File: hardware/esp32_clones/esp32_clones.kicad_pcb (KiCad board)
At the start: 2 copper layers, 110 x 60 mm, 27 parts, among them J2 USB_A, J3 USB_A, J4 USB_A, J5 Micro_SD_Card, J6 Barrel_Jack, J7 DA15_Pins, J9 AudioJack2_Ground

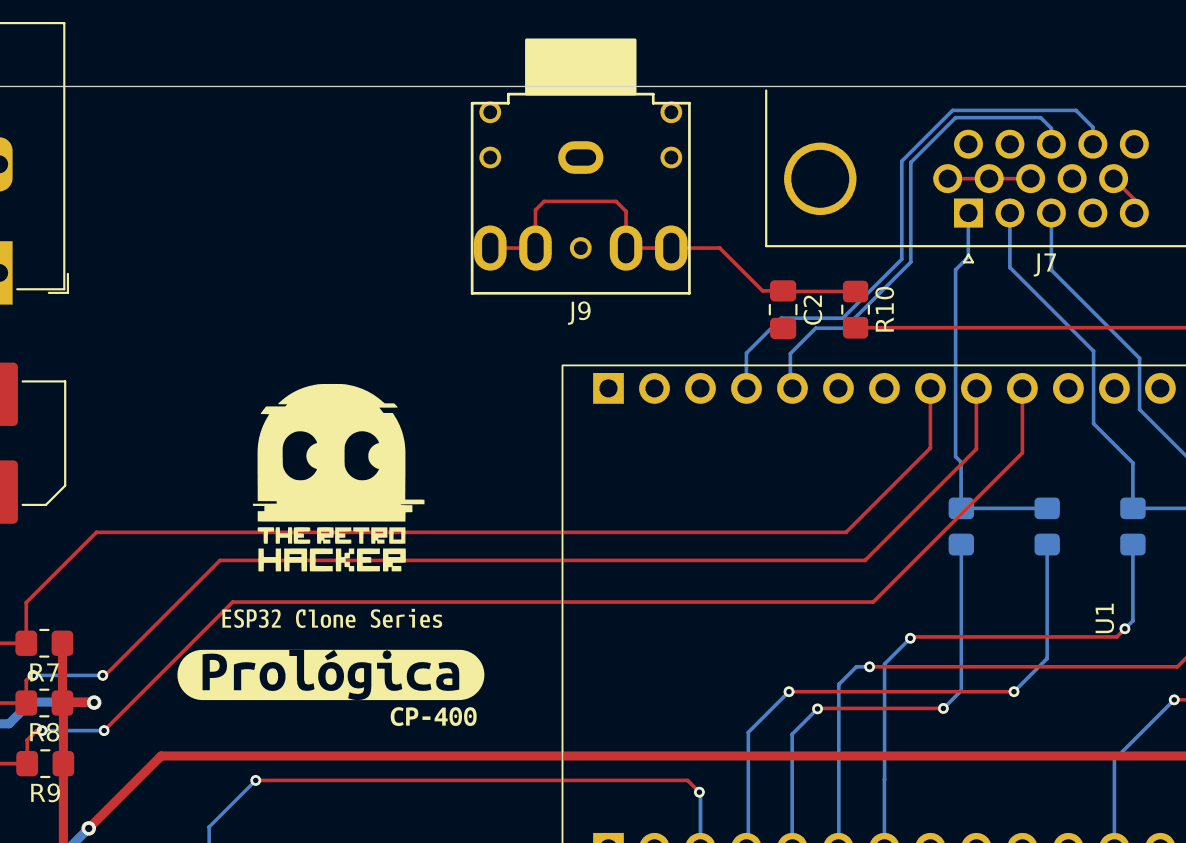
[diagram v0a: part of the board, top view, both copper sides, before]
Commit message: ## 1.11 - 2026-08-19
### Added

- Added a progress gauge that runs while a firmware update is validated and copied.

### Changed

- Moved the USB keyboard port to GPIO11 and GPIO12, joystick 1 to GPIO15 and GPIO16, and joystick 2 to GPIO17 and GPIO18, to simplify cable routing on the board.
- Gave every F12 screen the same layout, with the product name and screen title in the header, matching separator lines, and key hints in the footer. The disk image picker, firmware update screens, and error messages previously used their own styles.
- Renamed the "Joystick calibration" menu entry to "Joystick setup".
- Turned the joystick Serial debug output off by default.
- Listed only files with a matching extension when choosing a firmware or disk image, hiding folders such as System Volume Information that could not be opened anyway.
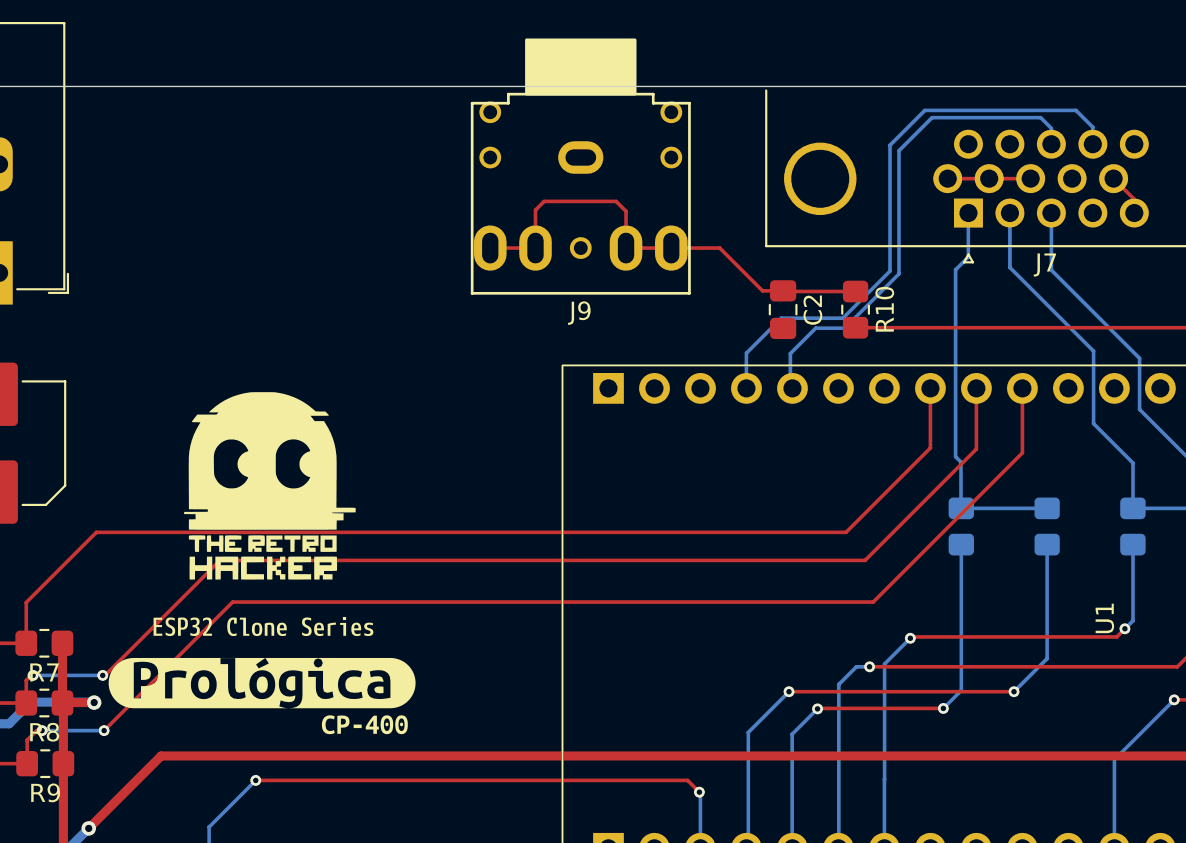
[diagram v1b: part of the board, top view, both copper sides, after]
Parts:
- moved G*** 3.83 mm to (124.6, 82.4)
- moved kibuzzard-6A32A22E 3.83 mm to (124.5, 93.0)
- moved kibuzzard-6A32A25A 3.83 mm to (124.5, 89.8)
- moved kibuzzard-6A32A222 3.83 mm to (130.2, 95.2)
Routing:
- net Net-(J7-P14): track 31.1 -> 32.0 mm
- net Net-(J7-P13): track 26.1 -> 26.9 mm
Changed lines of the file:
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@@
 	(footprint "kibuzzard-6A32A25A"
 		(layer "F.Cu")
-		(at 128.35 89.375)
+		(at 124.55 89.825)
 		(descr "Generated with KiBuzzard")
 		(tags "kb_params=eyJBbGlnbm1lbnRDaG9pY2UiOiAiQ2VudGVyIiwgIkNhcExlZnRDaG9pY2UiOiAiKCIsICJDYXBSaWdodENob2ljZSI6ICIpIiwgIkZvbnRDb21ib0JveCI6ICJtcGx1cy0xbW4tbWVkaXVtIiwgIkhlaWdodEN0cmwiOiAxLjAsICJMYXllckNvbWJvQm94IjogIkYuU2lsa1MiLCAiTGluZVNwYWNpbmdDdHJsIjogMTUuMCwgIk11bHRpTGluZVRleHQiOiAiRVNQMzIgQ2xvbmUgU2VyaWVzIiwgIlBhZGRpbmdCb3R0b21DdHJsIjogMC4wLCAiUGFkZGluZ0xlZnRDdHJsIjogMC4wLCAiUGFkZGluZ1JpZ2h0Q3RybCI6IDAuMCwgIlBhZGRpbmdUb3BDdHJsIjogMC4wLCAiV2lkdGhDdHJsIjogMC4wLCAiYWR2YW5jZWRDaGVja2JveCI6IHRydWUsICJpbmxpbmVGb3JtYXRUZXh0Ym94IjogdHJ1ZSwgImxpbmVvdmVyU3R5bGVDaG9pY2UiOiAiU3F1YXJlIiwgImxpbmVvdmVyVGhpY2tuZXNzQ3RybCI6IDV9")
@@
 	(footprint "TRH:TRH_NEW"
 		(layer "F.Cu")
-		(at 128.425 81.95)
+		(at 124.625 82.4)
 		(property "Reference" "G***"
 			(at 0 0 0)
@@
 	(footprint "kibuzzard-6A32A222"
 		(layer "F.Cu")
-		(at 133.95 94.8)
+		(at 130.15 95.25)
 		(descr "Generated with KiBuzzard")
 		(tags "kb_params=eyJBbGlnbm1lbnRDaG9pY2UiOiAiQ2VudGVyIiwgIkNhcExlZnRDaG9pY2UiOiAiKCIsICJDYXBSaWdodENob2ljZSI6ICIpIiwgIkZvbnRDb21ib0JveCI6ICJVYnVudHVNb25vLUIiLCAiSGVpZ2h0Q3RybCI6IDEuMCwgIkxheWVyQ29tYm9Cb3giOiAiRi5TaWxrUyIsICJMaW5lU3BhY2luZ0N0cmwiOiAxNS4wLCAiTXVsdGlMaW5lVGV4dCI6ICJDUC00MDAiLCAiUGFkZGluZ0JvdHRvbUN0cmwiOiAwLjAsICJQYWRkaW5nTGVmdEN0cmwiOiAwLjAsICJQYWRkaW5nUmlnaHRDdHJsIjogMC4wLCAiUGFkZGluZ1RvcEN0cmwiOiAwLjAsICJXaWR0aEN0cmwiOiAwLjAsICJhZHZhbmNlZENoZWNrYm94IjogdHJ1ZSwgImlubGluZUZvcm1hdFRleHRib3giOiB0cnVlLCAibGluZW92ZXJTdHlsZUNob2ljZSI6ICJTcXVhcmUiLCAibGluZW92ZXJUaGlja25lc3NDdHJsIjogNX0=")
@@
 	(footprint "kibuzzard-6A32A22E"
 		(layer "F.Cu")
-		(at 128.275 92.5)
+		(at 124.475 92.95)
 		(descr "Generated with KiBuzzard")
 		(tags "kb_params=eyJBbGlnbm1lbnRDaG9pY2UiOiAiQ2VudGVyIiwgIkNhcExlZnRDaG9pY2UiOiAiKCIsICJDYXBSaWdodENob2ljZSI6ICIpIiwgIkZvbnRDb21ib0JveCI6ICJVYnVudHVNb25vLUIiLCAiSGVpZ2h0Q3RybCI6IDIuMCwgIkxheWVyQ29tYm9Cb3giOiAiRi5TaWxrUyIsICJMaW5lU3BhY2luZ0N0cmwiOiAxNS4wLCAiTXVsdGlMaW5lVGV4dCI6ICJQcm9sXHUwMGYzZ2ljYSIsICJQYWRkaW5nQm90dG9tQ3RybCI6IDAuMCwgIlBhZGRpbmdMZWZ0Q3RybCI6IDAuMCwgIlBhZGRpbmdSaWdodEN0cmwiOiAwLjAsICJQYWRkaW5nVG9wQ3RybCI6IDAuMCwgIldpZHRoQ3RybCI6IDAuMCwgImFkdmFuY2VkQ2hlY2tib3giOiB0cnVlLCAiaW5saW5lRm9ybWF0VGV4dGJveCI6IGZhbHNlLCAibGluZW92ZXJTdHlsZUNob2ljZSI6ICJTcXVhcmUiLCAibGluZW92ZXJUaGlja25lc3NDdHJsIjogNX0=")
@@
 	)
 	(segment
-		(start 169.425 61.325)
-		(end 170.355 62.255)
+		(start 161.475 61.725)
+		(end 159.65 63.55)
 		(width 0.2)
 		(layer "B.Cu")
-		(net "Net-(J7-P14)")
+		(net "Net-(J7-P13)")
 	)
 	(segment
-		(start 151.225 76.675)
-		(end 151.225 74.725)
+		(start 153.65 74.75)
+		(end 153.65 76.56)
 		(width 0.2)
 		(layer "B.Cu")
-		(net "Net-(J7-P14)")
+		(net "Net-(J7-P13)")
 	)
 	(segment
-		(start 151.225 74.725)
-		(end 153.15 72.8)
+		(start 153.65 76.56)
+		(end 153.765 76.675)
 		(width 0.2)
 		(layer "B.Cu")
-		(net "Net-(J7-P14)")
+		(net "Net-(J7-P13)")
 	)
 	(segment
-		(start 162.609315 61.325)
-		(end 169.425 61.325)
+		(start 159.65 70.35)
+		(end 156.65 73.35)
 		(width 0.2)
 		(layer "B.Cu")
-		(net "Net-(J7-P14)")
+		(net "Net-(J7-P13)")
 	)
 	(segment
-		(start 153.15 72.8)
-		(end 156.55 72.8)
+		(start 159.65 63.55)
+		(end 159.65 70.35)
 		(width 0.2)
 		(layer "B.Cu")
-		(net "Net-(J7-P14)")
+		(net "Net-(J7-P13)")
 	)
 	(segment
-		(start 156.55 72.8)
-		(end 159.8 69.55)
+		(start 168.065 63.19)
+		(end 168.065 62.315)
 		(width 0.2)
 		(layer "B.Cu")
-		(net "Net-(J7-P14)")
+		(net "Net-(J7-P13)")
 	)
 	(segment
-		(start 170.355 62.255)
-		(end 170.355 63.19)
+		(start 156.65 73.35)
+		(end 155.05 73.35)
 		(width 0.2)
 		(layer "B.Cu")
-		(net "Net-(J7-P14)")
+		(net "Net-(J7-P13)")
 	)
 	(segment
-		(start 159.8 69.55)
-		(end 159.8 64.134315)
+		(start 155.05 73.35)
+		(end 153.65 74.75)
 		(width 0.2)
 		(layer "B.Cu")
-		(net "Net-(J7-P14)")
+		(net "Net-(J7-P13)")
 	)
 	(segment
-		(start 159.8 64.134315)
-		(end 162.609315 61.325)
+		(start 167.475 61.725)
+		(end 161.475 61.725)
 		(width 0.2)
 		(layer "B.Cu")
-		(net "Net-(J7-P14)")
+		(net "Net-(J7-P13)")
 	)
 	(segment
-		(start 153.65 74.75)
-		(end 153.65 76.56)
+		(start 168.065 62.315)
+		(end 167.475 61.725)
 		(width 0.2)
 		(layer "B.Cu")
@@
 	)
 	(segment
-		(start 162.775 61.725)
-		(end 160.3 64.2)
+		(start 153.15 72.8)
+		(end 156.55 72.8)
 		(width 0.2)
 		(layer "B.Cu")
-		(net "Net-(J7-P13)")
+		(net "Net-(J7-P14)")
 	)
 	(segment
-		(start 153.65 76.56)
-		(end 153.765 76.675)
+		(start 161.075 61.325)
+		(end 169.425 61.325)
 		(width 0.2)
 		(layer "B.Cu")
-		(net "Net-(J7-P13)")
+		(net "Net-(J7-P14)")
 	)
 	(segment
-		(start 155.05 73.35)
-		(end 153.65 74.75)
+		(start 169.425 61.325)
+		(end 170.355 62.255)
 		(width 0.2)
 		(layer "B.Cu")
-		(net "Net-(J7-P13)")
+		(net "Net-(J7-P14)")
 	)
 	(segment
-		(start 160.3 64.2)
-		(end 160.3 69.7)
+		(start 151.225 74.725)
+		(end 153.15 72.8)
 		(width 0.2)
 		(layer "B.Cu")
-		(net "Net-(J7-P13)")
+		(net "Net-(J7-P14)")
 	)
 	(segment
-		(start 168.065 63.19)
-		(end 168.065 62.315)
+		(start 170.355 62.255)
+		(end 170.355 63.19)
 		(width 0.2)
 		(layer "B.Cu")
-		(net "Net-(J7-P13)")
+		(net "Net-(J7-P14)")
 	)
 	(segment
-		(start 156.65 73.35)
-		(end 155.05 73.35)
+		(start 151.225 76.675)
+		(end 151.225 74.725)
 		(width 0.2)
 		(layer "B.Cu")
-		(net "Net-(J7-P13)")
+		(net "Net-(J7-P14)")
 	)
 	(segment
-		(start 167.475 61.725)
-		(end 162.775 61.725)
+		(start 159.15 70.2)
+		(end 159.15 63.25)
 		(width 0.2)
 		(layer "B.Cu")
-		(net "Net-(J7-P13)")
+		(net "Net-(J7-P14)")
 	)
 	(segment
-		(start 160.3 69.7)
-		(end 156.65 73.35)
+		(start 156.55 72.8)
+		(end 159.15 70.2)
 		(width 0.2)
 		(layer "B.Cu")
-		(net "Net-(J7-P13)")
+		(net "Net-(J7-P14)")
 	)
 	(segment
-		(start 168.065 62.315)
-		(end 167.475 61.725)
+		(start 159.15 63.25)
+		(end 161.075 61.325)
 		(width 0.2)
 		(layer "B.Cu")
-		(net "Net-(J7-P13)")
+		(net "Net-(J7-P14)")
 	)
 	(segment

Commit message: Refactor code structure for improved readability and maintainability
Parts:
- J2: value USB_A -> Joystick 2
- J3: value USB_A -> Joystick 1
- J4: value USB_A -> Keyboard
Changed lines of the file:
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@@
 		(at 177.725 113.495)
 		(property "Reference" "J4"
-			(at -1.90748 -5.46808 0)
+			(at -8.275 4.855 0)
 			(layer "F.SilkS")
 			(effects
@@
 			)
 		)
-		(property "Value" "USB_A"
-			(at 4.32453 11.828855 0)
+		(property "Value" "Keyboard"
+			(at 0.025 -5.295 0)
 			(layer "F.Fab")
 			(effects
@@
 		(at 157.425 113.495)
 		(property "Reference" "J2"
-			(at -1.90748 -5.46808 0)
+			(at -8.175 4.905 0)
 			(layer "F.SilkS")
 			(effects
@@
 			)
 		)
-		(property "Value" "USB_A"
-			(at 4.32453 11.828855 0)
+		(property "Value" "Joystick 2"
+			(at -0.025 -5.295 0)
 			(layer "F.Fab")
 			(effects
@@
 		(at 137.125 113.495)
 		(property "Reference" "J3"
-			(at -1.90748 -5.46808 0)
+			(at -8.375 4.805 0)
 			(layer "F.SilkS")
 			(effects
@@
 			)
 		)
-		(property "Value" "USB_A"
-			(at 4.32453 11.828855 0)
-			(layer "F.Fab")
-			(effects
-				(font
+		(property "Value" "Joystick 1"
+			(at 0.025 -5.295 0)
+			(layer "F.SilkS")
+			(effects
+				(font

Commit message: Add USB-OTG host support for CP400 keyboard
- Implemented CP400UsbKeyboard.cpp to manage USB keyboard connections using the ESP32-S3 USB-OTG controller.
- Created CP400UsbKeyboard.h header file to declare functions for starting the USB keyboard and checking connection status.
- The new implementation allows for full-speed keyboard enumeration and improves compatibility with various USB keyboards.
- Hardware revision 1.2
- Moved the keyboard port to the ESP32-S3 native USB-OTG host on GPIO19 and GPIO20, so ordinary full speed USB keyboards now work. The previous bit-banged stack could only talk to low speed devices, which is why most keyboards appeared dead or never lit their indicators.
- Requested the HID boot protocol from the keyboard, so keyboards that default to their own report layout still deliver the standard report the emulator expects.
- Turned the native USB serial console off, because the keyboard host and the console cannot share the one USB controller. Serial output and firmware uploads now use the UART port, which already carried the boot log.
- Kept joystick 1 and joystick 2 on the existing bit-banged stack, unchanged.
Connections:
- J2 pad 1: +3.3V -> +5V
- J3 pad 1: +3.3V -> +5V
- J4 pad 1: +3.3V -> +5V
- U1 pad 3: unconnected-(U1-IO19-Pad3) -> Net-(J4-D-)
- U1 pad 39: Net-(J4-D-) -> unconnected-(U1-IO11-Pad39)
- U1 pad 4: unconnected-(U1-I020-Pad4) -> Net-(J4-D+)
- U1 pad 40: Net-(J4-D+) -> unconnected-(U1-IO12-Pad40)
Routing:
- net +5V: track 127.3 -> 201.2 mm
- net +3.3V: track 109.2 -> 59.0 mm
- net Net-(J4-D-): track 14.3 -> 44.7 mm, vias 0 -> 1
- net Net-(J4-D+): track 14.8 -> 44.0 mm, vias 0 -> 1
